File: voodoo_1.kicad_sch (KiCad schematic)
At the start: 1 part, among them U1 LM301

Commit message: 回路図作成
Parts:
- added C1: 22p, symbol Device:C
- added C10, C4, C9: 0.1u, symbol Device:C
- added C2, C5: 2.2u, symbol Device:C_US
- added C3: 22u, symbol Device:C_US
- added C6, C7, C8: 100u, symbol Device:C
- added D1, D2, D3, D4: 1N4148WT, Diode_SMD:D_SOD-523, symbol Diode:1N4148WT
- added Q1, Q2: BC549, Package_TO_SOT_THT:TO-92_Inline, symbol Transistor_BJT:BC549
- added R1: 150k, symbol Device:R
- added R10: 70k, symbol Device:R
- added R11: 1.5k, symbol Device:R
- added R12, R13: 39k, symbol Device:R
- added R14: 12k, symbol Device:R
- added R15: 820k, symbol Device:R
- added R16: 1M, symbol Device:R
- added R17, R18: 10k, symbol Device:R
- added R2: 39, symbol Device:R
- added R3, R4: 47k, symbol Device:R
- added R5: 22k, symbol Device:R
- added R6, R7: 680k, symbol Device:R
- added R9: 2.2M, symbol Device:R
- added RV1: 50k, symbol Device:R_Potentiometer
- added RV2, RV3: 100k, symbol Device:R_Potentiometer
- added SW1: SW_DPDT_x2, symbol Switch:SW_DPDT_x2
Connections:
- net at U1.1 (COMP1): now also U1.6, C1.1, C5.1, R1.2
- net at U1.2 (-): now also C2.1, R1.1
- net at U1.3 (+): now also Q1.1 (C), R4.1
- net +9V: now reaches U1.7 (V+)
- net +9V: now also Q2.1 (C), R15.2, R3.2
- net at U1.8 (COMP2): now also C1.2
- new net: D1.1 (K), D2.2 (A), D3.1 (K), D4.2 (A)
- new net: D1.2 (A), D4.1 (K), R10.2, R11.1
- new net: C6.2, C7.1, R11.2, R12.1
- new net: C8.1, R12.2, R14.1, R14.2, RV2.3
- new net: C6.1, R13.2, RV2.1
- new net: C9.1, Q2.2 (B), R15.1, R16.2
- new net: RV2.2, RV3.1
- new net: C9.2, RV3.2
- new net: C4.1, Q1.2 (B), R6.2, R7.1, SW1.6 (C)
- new net: C3.1, R3.1, R4.2, R7.2
- new net: C10.1, R18.2, SW1.4 (A)
- new net: C10.2, Q2.3 (E), R17.2
- new net: C5.2, R10.1
- new net: C2.2, R2.1
- new net: R2.2, RV1.2
- new net: C4.2, R9.2, SW1.1 (A)
- new net: Q1.3 (E), R5.2
- new net GND: C3.2, C7.2, C8.2, D2.1 (K), D3.2 (A), R13.1, R16.1, R17.1, R18.1, R5.1, R6.1, R9.1, RV1.3, RV3.3
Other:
- moved on the sheet: U1

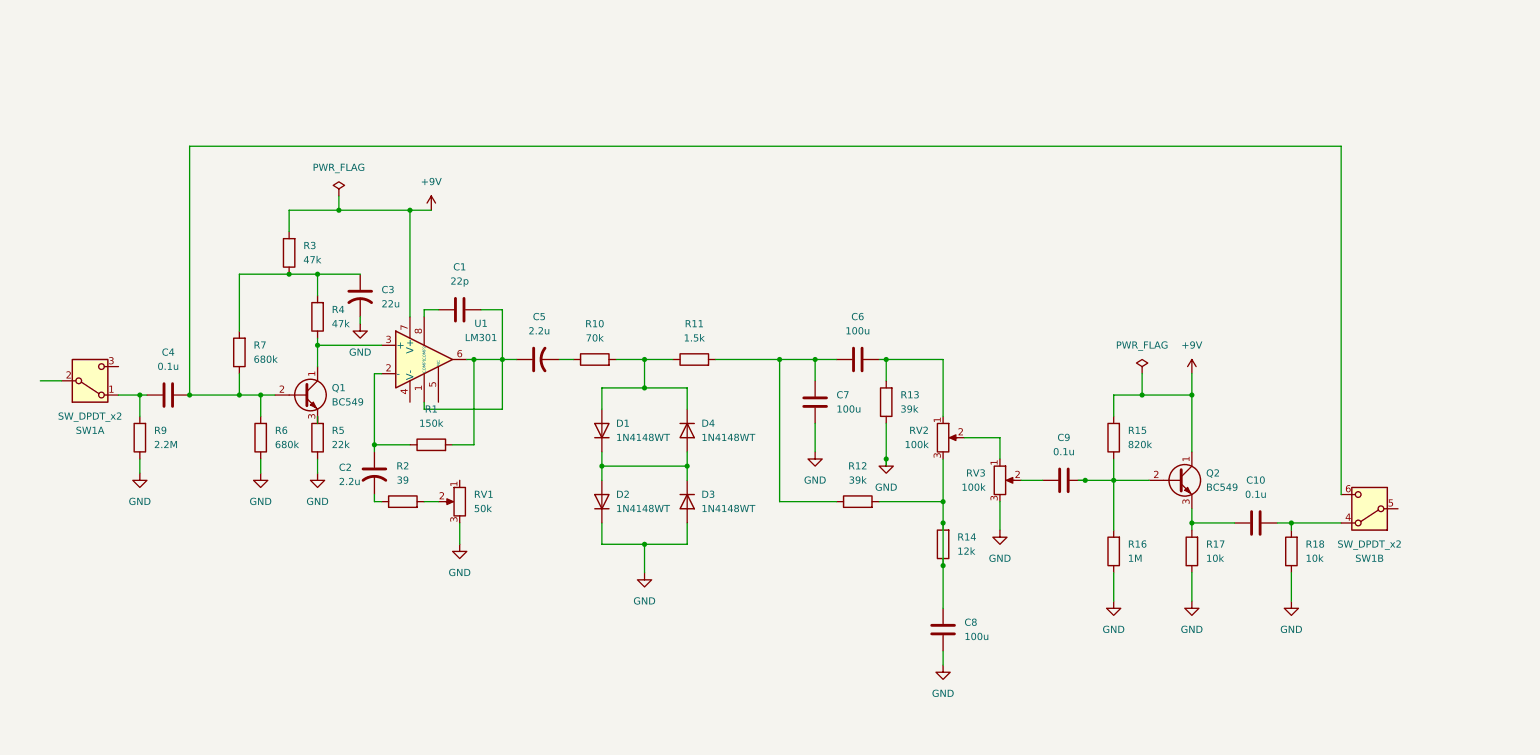
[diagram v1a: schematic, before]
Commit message: フットプリント割り当て
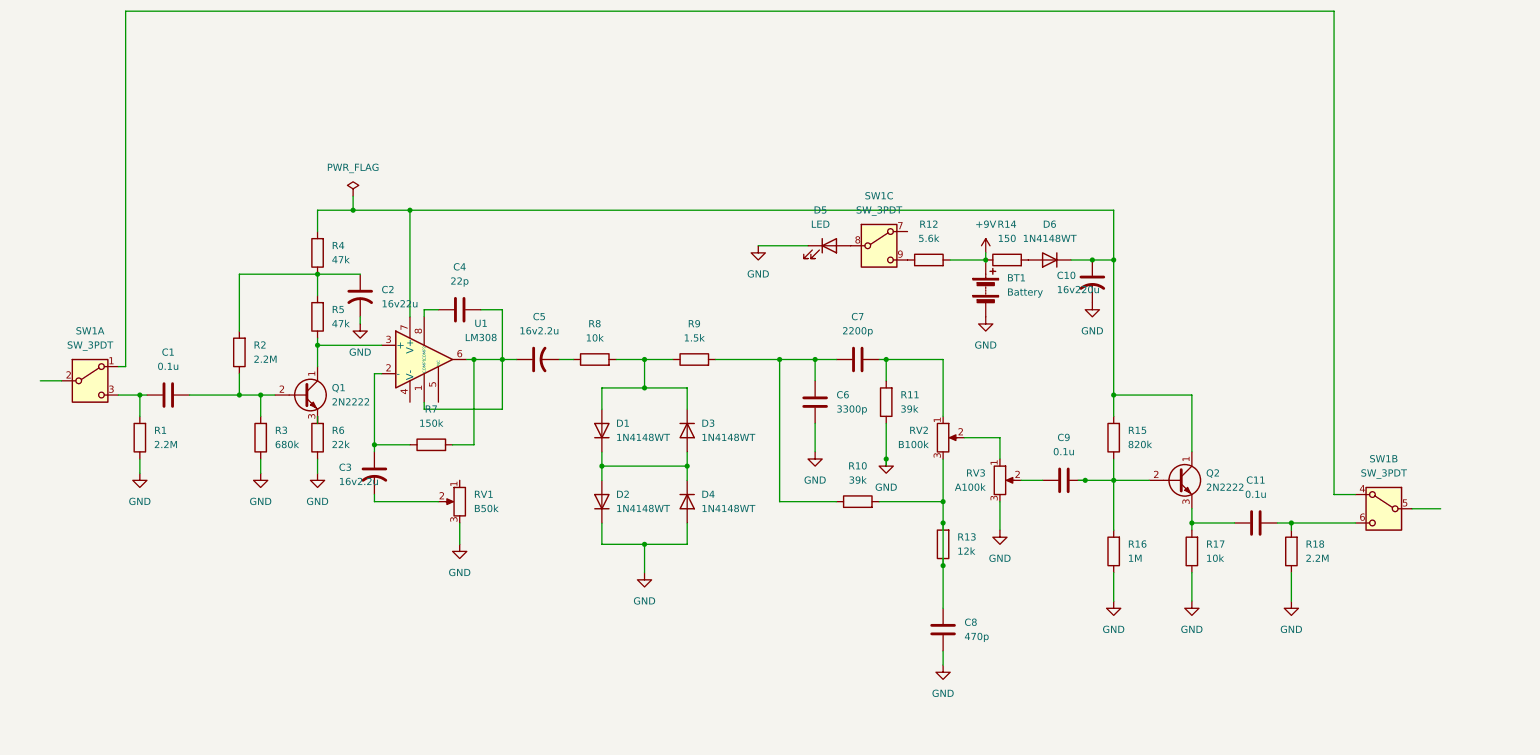
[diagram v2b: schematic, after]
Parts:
- removed R2: 39, symbol Device:R
- removed SW1: SW_DPDT_x2, symbol Switch:SW_DPDT_x2
- added BT1: Battery, symbol Device:Battery
- added C10: 16v220u, Capacitor_THT:CP_Radial_D7.5mm_P2.50mm, symbol Device:C_US
- added D5: LED, symbol Device:LED
- added D6: 1N4148WT, Diode_SMD:D_SOD-523, symbol Diode:1N4148WT
- added R12: 5.6k, Resistor_THT:R_Axial_DIN0207_L6.3mm_D2.5mm_P7.62mm_Horizontal, symbol Device:R
- added R14: 150, Resistor_THT:R_Axial_DIN0207_L6.3mm_D2.5mm_P7.62mm_Horizontal, symbol Device:R
- added SW1: SW_3PDT, symbol @MyLibrary:SW_3PDT
- C1: renamed from C4; footprint (none) -> Capacitor_THT:C_Disc_D6.0mm_W2.5mm_P5.00mm
- C11: renamed from C10; footprint (none) -> Capacitor_THT:C_Disc_D6.0mm_W2.5mm_P5.00mm
- C2: renamed from C3; value 22u -> 16v22u; footprint (none) -> Capacitor_THT:CP_Radial_D6.3mm_P2.50mm
- C3: renamed from C2; value 2.2u -> 16v2.2u; footprint (none) -> Capacitor_THT:CP_Radial_D6.3mm_P2.50mm
- C4: renamed from C1; footprint (none) -> Capacitor_THT:C_Disc_D4.3mm_W1.9mm_P5.00mm
- C5: value 2.2u -> 16v2.2u; footprint (none) -> Capacitor_THT:CP_Radial_D6.3mm_P2.50mm
- C6: renamed from C7; value 100u -> 3300p; footprint (none) -> Capacitor_THT:C_Disc_D4.3mm_W1.9mm_P5.00mm
- C7: renamed from C6; value 100u -> 2200p; footprint (none) -> Capacitor_THT:C_Disc_D4.3mm_W1.9mm_P5.00mm
- C8: value 100u -> 470p; footprint (none) -> Capacitor_THT:C_Disc_D4.3mm_W1.9mm_P5.00mm
- C9: footprint (none) -> Capacitor_THT:C_Disc_D6.0mm_W2.5mm_P5.00mm
- D1, D2: footprint Diode_SMD:D_SOD-523 -> Diode_THT:D_DO-35_SOD27_P10.16mm_Horizontal
- D3: renamed from D4; footprint Diode_SMD:D_SOD-523 -> Diode_THT:D_DO-35_SOD27_P10.16mm_Horizontal
- D4: renamed from D3; footprint Diode_SMD:D_SOD-523 -> Diode_THT:D_DO-35_SOD27_P10.16mm_Horizontal
- Q1, Q2: value BC549 -> 2N2222
- R1: renamed from R9; footprint (none) -> Resistor_THT:R_Axial_DIN0207_L6.3mm_D2.5mm_P7.62mm_Horizontal
- R10: renamed from R12; footprint (none) -> Resistor_THT:R_Axial_DIN0207_L6.3mm_D2.5mm_P7.62mm_Horizontal
- R11: renamed from R13; footprint (none) -> Resistor_THT:R_Axial_DIN0207_L6.3mm_D2.5mm_P7.62mm_Horizontal
- R13: renamed from R14; footprint (none) -> Resistor_THT:R_Axial_DIN0207_L6.3mm_D2.5mm_P7.62mm_Horizontal
- R15, R16, R17: footprint (none) -> Resistor_THT:R_Axial_DIN0207_L6.3mm_D2.5mm_P7.62mm_Horizontal
- R18: value 10k -> 2.2M; footprint (none) -> Resistor_THT:R_Axial_DIN0207_L6.3mm_D2.5mm_P7.62mm_Horizontal
- R2: renamed from R7; value 680k -> 2.2M; footprint (none) -> Resistor_THT:R_Axial_DIN0207_L6.3mm_D2.5mm_P7.62mm_Horizontal
- R3: renamed from R6; footprint (none) -> Resistor_THT:R_Axial_DIN0207_L6.3mm_D2.5mm_P7.62mm_Horizontal
- R4: renamed from R3; footprint (none) -> Resistor_THT:R_Axial_DIN0207_L6.3mm_D2.5mm_P7.62mm_Horizontal
- R5: renamed from R4; footprint (none) -> Resistor_THT:R_Axial_DIN0207_L6.3mm_D2.5mm_P7.62mm_Horizontal
- R6: renamed from R5; footprint (none) -> Resistor_THT:R_Axial_DIN0207_L6.3mm_D2.5mm_P7.62mm_Horizontal
- R7: renamed from R1; footprint (none) -> Resistor_THT:R_Axial_DIN0207_L6.3mm_D2.5mm_P7.62mm_Horizontal
- R8: renamed from R10; value 70k -> 10k; footprint (none) -> Resistor_THT:R_Axial_DIN0207_L6.3mm_D2.5mm_P7.62mm_Horizontal
- R9: renamed from R11; footprint (none) -> Resistor_THT:R_Axial_DIN0207_L6.3mm_D2.5mm_P7.62mm_Horizontal
- RV1: value 50k -> B50k
- RV2: value 100k -> B100k
- RV3: value 100k -> A100k
- U1: value LM301 -> LM308
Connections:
- net +9V: now also BT1.1 (+), R12.2, R14.1; no longer Q2.1 (C), R15.2, R4.2, U1.7 (V+)
- net GND: now also BT1.2 (-), C10.2, D5.1 (K)
- net at C11.1, R18.2: now also SW1.6 (C)
- net at C3.2: now also RV1.2
- net at C1.2, R1.2: now also SW1.3 (C)
- new net: C10.1, D6.1 (K), Q2.1 (C), R15.2, R4.2, U1.7 (V+)
- new net: D6.2 (A), R14.2
- new net: SW1.1 (A), SW1.4 (A)
- new net: R12.1, SW1.9 (C)
- new net: D5.2 (A), SW1.8 (B)
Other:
- moved on the sheet: R4

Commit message: 部品を配置
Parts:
- removed D6: 1N4148WT, Diode_SMD:D_SOD-523, symbol Diode:1N4148WT
- added D6: 1N4001, Diode_THT:D_DO-41_SOD81_P10.16mm_Horizontal, symbol Diode:1N4001
- Q1, Q2: footprint Package_TO_SOT_THT:TO-92_Inline -> Package_TO_SOT_THT:TO-92_Wide
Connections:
- net at C5.1, R7.2, U1.6: no longer C4.1, U1.1 (COMP1)
- net at R10.2, R13.2, RV2.3: no longer C8.1, R13.1
- net at C10.1, Q2.1 (C), R15.2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: now also D6.1 (K)
- net at R14.2: now also D6.2 (A)
- net at C3.2, RV1.2: now also RV1.1
- new net: C4.1, U1.1 (COMP1)
- new net: C8.1, R13.1
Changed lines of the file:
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@@
 	)
 	(junction
-		(at 177.8 114.3)
+		(at 177.8 110.49)
 		(diameter 0)
 		(color 0 0 0 0)
@@
 	)
 	(junction
-		(at 204.47 67.31)
-		(diameter 0)
-		(color 0 0 0 0)
-	)
-	(junction
 		(at 34.29 91.44)
 		(diameter 0)
@@
 	)
 	(junction
-		(at 99.06 85.09)
+		(at 204.47 67.31)
 		(diameter 0)
 		(color 0 0 0 0)
@@
 	)
 	(junction
-		(at 177.8 121.92)
-		(diameter 0)
-		(color 0 0 0 0)
-	)
-	(junction
 		(at 185.42 67.31)
 		(diameter 0)
@@
 	)
 	(junction
-		(at 177.8 110.49)
+		(at 85.09 110.49)
 		(diameter 0)
 		(color 0 0 0 0)
@@
 	(wire
 		(pts
-			(xy 208.28 67.31) (xy 208.28 91.44)
-		)
-		(stroke
-			(width 0)
-			(type default)
-		)
-	)
-	(wire
-		(pts
 			(xy 109.22 85.09) (xy 111.76 85.09)
 		)
@@
 	(wire
 		(pts
+			(xy 99.06 76.2) (xy 99.06 93.98)
+		)
+		(stroke
+			(width 0)
+			(type default)
+		)
+	)
+	(wire
+		(pts
 			(xy 66.04 82.55) (xy 77.47 82.55)
 		)
@@
 	(wire
 		(pts
+			(xy 85.09 110.49) (xy 87.63 110.49)
+		)
+		(stroke
+			(width 0)
+			(type default)
+		)
+	)
+	(wire
+		(pts
 			(xy 185.42 67.31) (xy 185.42 66.04)
 		)
@@
 	(wire
 		(pts
-			(xy 240.03 114.3) (xy 251.46 114.3)
+			(xy 208.28 67.31) (xy 208.28 91.44)
 		)
 		(stroke
@@
 	(wire
 		(pts
-			(xy 208.28 123.19) (xy 208.28 128.27)
+			(xy 240.03 114.3) (xy 251.46 114.3)
 		)
 		(stroke
@@
 	(wire
 		(pts
-			(xy 177.8 121.92) (xy 177.8 114.3)
+			(xy 208.28 123.19) (xy 208.28 128.27)
 		)
 		(stroke
@@
 	(wire
 		(pts
-			(xy 204.47 67.31) (xy 208.28 67.31)
+			(xy 85.09 106.68) (xy 85.09 110.49)
 		)
 		(stroke
@@
 	(wire
 		(pts
-			(xy 99.06 85.09) (xy 99.06 93.98)
+			(xy 208.28 58.42) (xy 208.28 67.31)
 		)
 		(stroke
@@
 	(wire
 		(pts
-			(xy 208.28 58.42) (xy 208.28 67.31)
+			(xy 124.46 118.11) (xy 132.08 118.11)
 		)
 		(stroke
@@
 	(wire
 		(pts
-			(xy 124.46 118.11) (xy 132.08 118.11)
+			(xy 177.8 121.92) (xy 177.8 129.54)
 		)
 		(stroke
@@
 	(wire
 		(pts
-			(xy 76.2 110.49) (xy 87.63 110.49)
+			(xy 76.2 110.49) (xy 85.09 110.49)
 		)
 		(stroke
@@
 	(wire
 		(pts
-			(xy 95.25 76.2) (xy 99.06 76.2)
+			(xy 204.47 67.31) (xy 208.28 67.31)
 		)
 		(stroke
@@
 	(wire
 		(pts
-			(xy 93.98 85.09) (xy 99.06 85.09)
+			(xy 95.25 76.2) (xy 99.06 76.2)
 		)
 		(stroke
@@
 	(wire
 		(pts
-			(xy 31.75 22.86) (xy 31.75 86.36)
+			(xy 93.98 85.09) (xy 101.6 85.09)
 		)
 		(stroke
@@
 	(wire
 		(pts
-			(xy 167.64 85.09) (xy 177.8 85.09)
+			(xy 31.75 22.86) (xy 31.75 86.36)
 		)
 		(stroke
@@
 	(wire
 		(pts
-			(xy 99.06 76.2) (xy 99.06 85.09)
+			(xy 167.64 85.09) (xy 177.8 85.09)
 		)
 		(stroke
@@
 	(wire
 		(pts
-			(xy 187.96 110.49) (xy 187.96 115.57)
+			(xy 91.44 106.68) (xy 85.09 106.68)
 		)
 		(stroke
@@
 	(wire
 		(pts
-			(xy 99.06 85.09) (xy 101.6 85.09)
+			(xy 187.96 110.49) (xy 187.96 115.57)
 		)
 		(stroke
@@
 	(wire
 		(pts
-			(xy 177.8 121.92) (xy 177.8 129.54)
-		)
-		(stroke
-			(width 0)
-			(type default)
-		)
-	)
-	(wire
-		(pts
 			(xy 119.38 85.09) (xy 124.46 85.09)
 		)
@@
 	)
 	(symbol
-		(lib_id "Diode:1N4148WT")
-		(at 196.85 67.31 180)
-		(unit 1)
-		(exclude_from_sim no)
-		(in_bom yes)
-		(on_board yes)
-		(dnp no)
-		(fields_autoplaced yes)
-		(property "Reference" "D6"
-			(at 196.85 60.96 0)
-			(effects
-				(font
-					(size 1.27 1.27)
-				)
-			)
-		)
-		(property "Value" "1N4148WT"
-			(at 196.85 63.5 0)
-			(effects
-				(font
-					(size 1.27 1.27)
-				)
-			)
-		)
-		(property "Footprint" "Diode_SMD:D_SOD-523"
-			(at 196.85 62.865 0)
-			(effects
-				(font
-					(size 1.27 1.27)
-				)
-				(hide yes)
-			)
-		)
-		(property "Datasheet" "https://www.diodes.com/assets/Datasheets/ds30396.pdf"
-			(at 196.85 67.31 0)
-			(effects
-				(font
-					(size 1.27 1.27)
-				)
-				(hide yes)
-			)
-		)
-		(property "Description" "75V 0.15A Fast switching Diode, SOD-523"
-			(at 196.85 67.31 0)
-			(effects
-				(font
-					(size 1.27 1.27)
-				)
-				(hide yes)
-			)
-		)
-		(property "Sim.Device" "D"
-			(at 196.85 67.31 0)
-			(effects
-				(font
-					(size 1.27 1.27)
-				)
-				(hide yes)
-			)
-		)
-		(property "Sim.Pins" "1=K 2=A"
-			(at 196.85 67.31 0)
-			(effects
-				(font
-					(size 1.27 1.27)
-				)
-				(hide yes)
-			)
-		)
-		(pin "1"
-		)
-		(pin "2"
-		)
-		(instances
-			(project "voodoo_1"
-				(path "/17f12b88-d15e-422f-90d6-d6611e595670"
-					(reference "D6")
-					(unit 1)
-				)
-			)
-		)
-	)
-	(symbol
 		(lib_id "@MyLibrary:SW_3PDT")
 		(at 25.4 88.9 0)
@@
 			)
 		)
-		(property "Footprint" "Package_TO_SOT_THT:TO-92_Inline"
+		(property "Footprint" "Package_TO_SOT_THT:TO-92_Wide"
 			(at 224.79 108.585 0)
 			(effects
@@
 	)
 	(symbol
+		(lib_id "Diode:1N4001")
+		(at 196.85 67.31 180)
+		(unit 1)
+		(exclude_from_sim no)
+		(in_bom yes)
+		(on_board yes)
+		(dnp no)
+		(fields_autoplaced yes)
+		(property "Reference" "D6"
+			(at 196.85 60.96 0)
+			(effects
+				(font
+					(size 1.27 1.27)
+				)
+			)
+		)
+		(property "Value" "1N4001"
+			(at 196.85 63.5 0)
+			(effects
+				(font
+					(size 1.27 1.27)
+				)
+			)
+		)
+		(property "Footprint" "Diode_THT:D_DO-41_SOD81_P10.16mm_Horizontal"
+			(at 196.85 67.31 0)
+			(effects
+				(font
+					(size 1.27 1.27)
+				)
+				(hide yes)
+			)
+		)
+		(property "Datasheet" "http://www.vishay.com/docs/88503/1n4001.pdf"
+			(at 196.85 67.31 0)
+			(effects
+				(font
+					(size 1.27 1.27)
+				)
+				(hide yes)
+			)
+		)
+		(property "Description" "50V 1A General Purpose Rectifier Diode, DO-41"
+			(at 196.85 67.31 0)
+			(effects
+				(font
+					(size 1.27 1.27)
+				)
+				(hide yes)
+			)
+		)
+		(property "Sim.Device" "D"
+			(at 196.85 67.31 0)
+			(effects
+				(font
+					(size 1.27 1.27)
+				)
+				(hide yes)
+			)
+		)
+		(property "Sim.Pins" "1=K 2=A"
+			(at 196.85 67.31 0)
+			(effects
+				(font
+					(size 1.27 1.27)
+				)
+				(hide yes)
+			)
+		)
+		(pin "1"
+		)
+		(pin "2"
+		)
+		(instances
+			(project ""
+				(path "/17f12b88-d15e-422f-90d6-d6611e595670"
+					(reference "D6")
+					(unit 1)
+				)
+			)
+		)
+	)
+	(symbol
 		(lib_id "Device:R")
 		(at 162.56 110.49 90)
@@
 			)
 		)
-		(property "Footprint" "Package_TO_SOT_THT:TO-92_Inline"
+		(property "Footprint" "Package_TO_SOT_THT:TO-92_Wide"
 			(at 68.58 93.345 0)
 			(effects

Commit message: 4番ピンがGNDに接続されてなかった
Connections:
- net GND: now also U1.4 (V-)
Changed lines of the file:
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@@
+	)
+	(symbol
+		(lib_id "power:GND")
+		(at 82.55 92.71 0)
+		(unit 1)
+		(exclude_from_sim no)
+		(in_bom yes)
+		(on_board yes)
+		(dnp no)
+		(fields_autoplaced yes)
+		(property "Reference" "#PWR018"
+			(at 82.55 99.06 0)
+			(effects
+				(font
+					(size 1.27 1.27)
+				)
+				(hide yes)
+			)
+		)
+		(property "Value" "GND"
+			(at 82.55 97.79 0)
+			(effects
+				(font
+					(size 1.27 1.27)
+				)
+			)
+		)
+		(property "Footprint" ""
+			(at 82.55 92.71 0)
+			(effects
+				(font
+					(size 1.27 1.27)
+				)
+				(hide yes)
+			)
+		)
+		(property "Datasheet" ""
+			(at 82.55 92.71 0)
+			(effects
+				(font
+					(size 1.27 1.27)
+				)
+				(hide yes)
+			)
+		)
+		(property "Description" "Power symbol creates a global label with name \"GND\" , ground"
+			(at 82.55 92.71 0)
+			(effects
+				(font
+					(size 1.27 1.27)
+				)
+				(hide yes)
+			)
+		)
+		(pin "1"
+		)
+		(instances
+			(project "voodoo_1"
+				(path "/17f12b88-d15e-422f-90d6-d6611e595670"
+					(reference "#PWR018")
+					(unit 1)
+				)
+			)
+		)
 	)
 	(symbol
